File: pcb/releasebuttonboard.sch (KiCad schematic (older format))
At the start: 24 parts

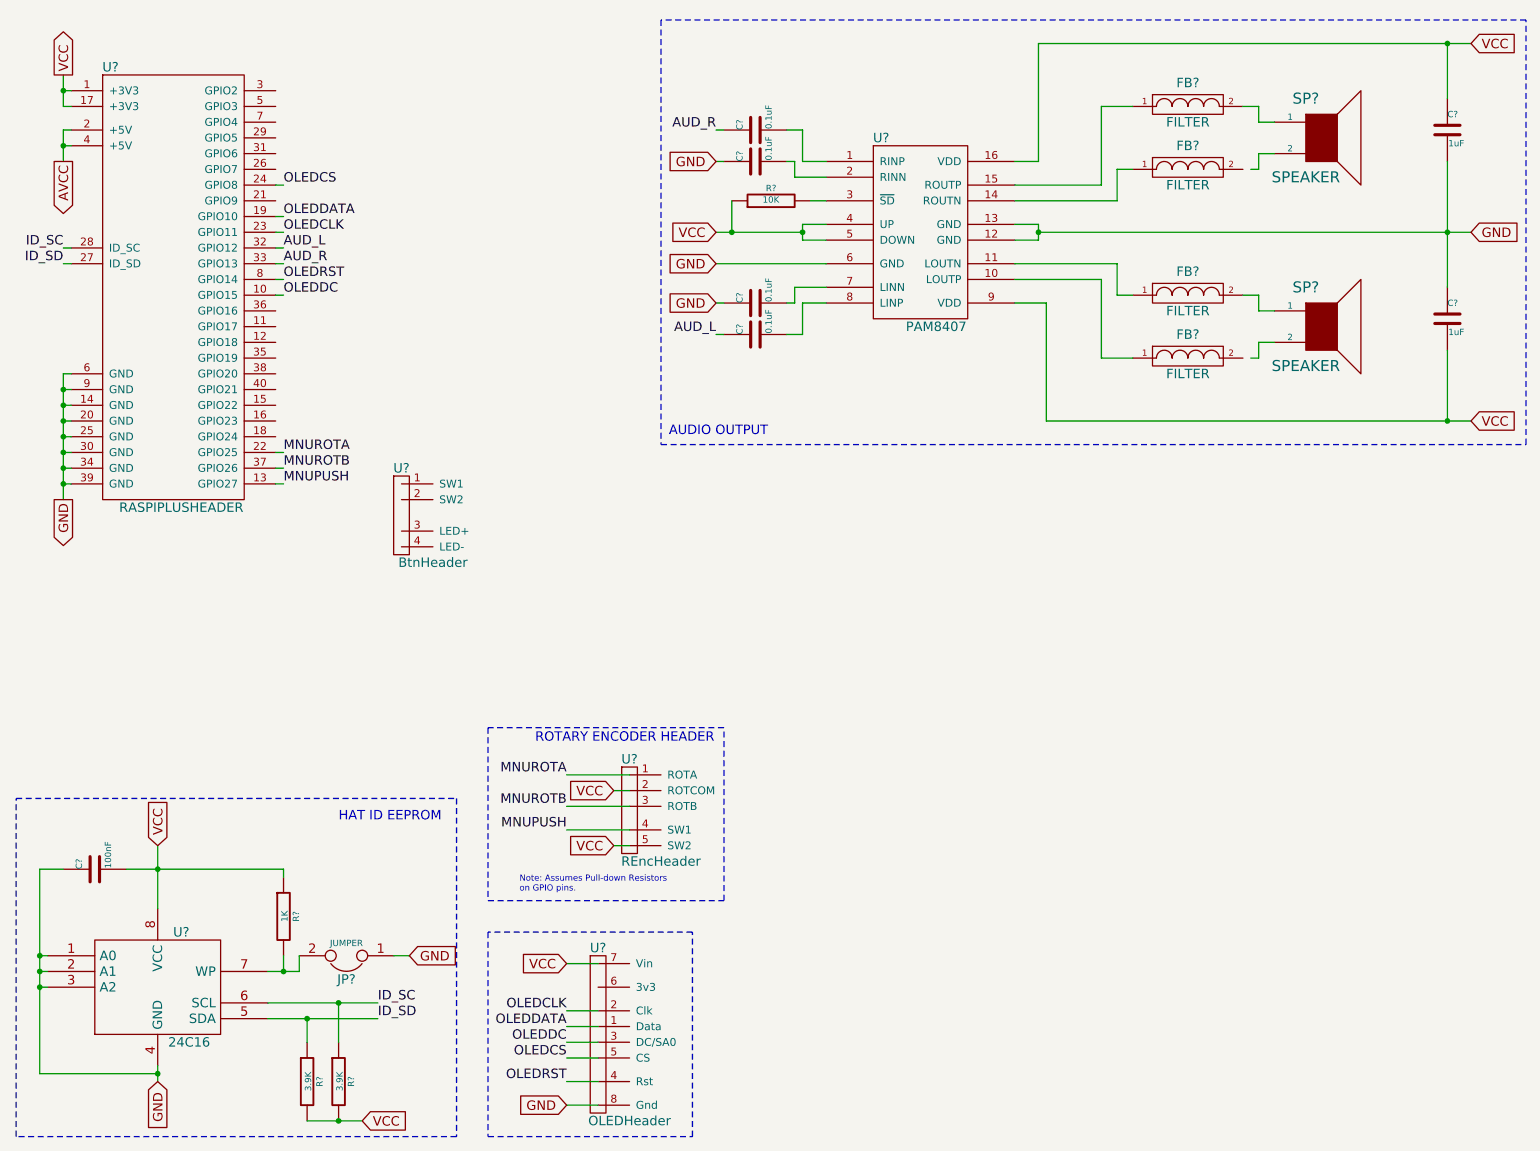
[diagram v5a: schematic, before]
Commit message: Header for big button.
(Plus misc schematic layout changes.)
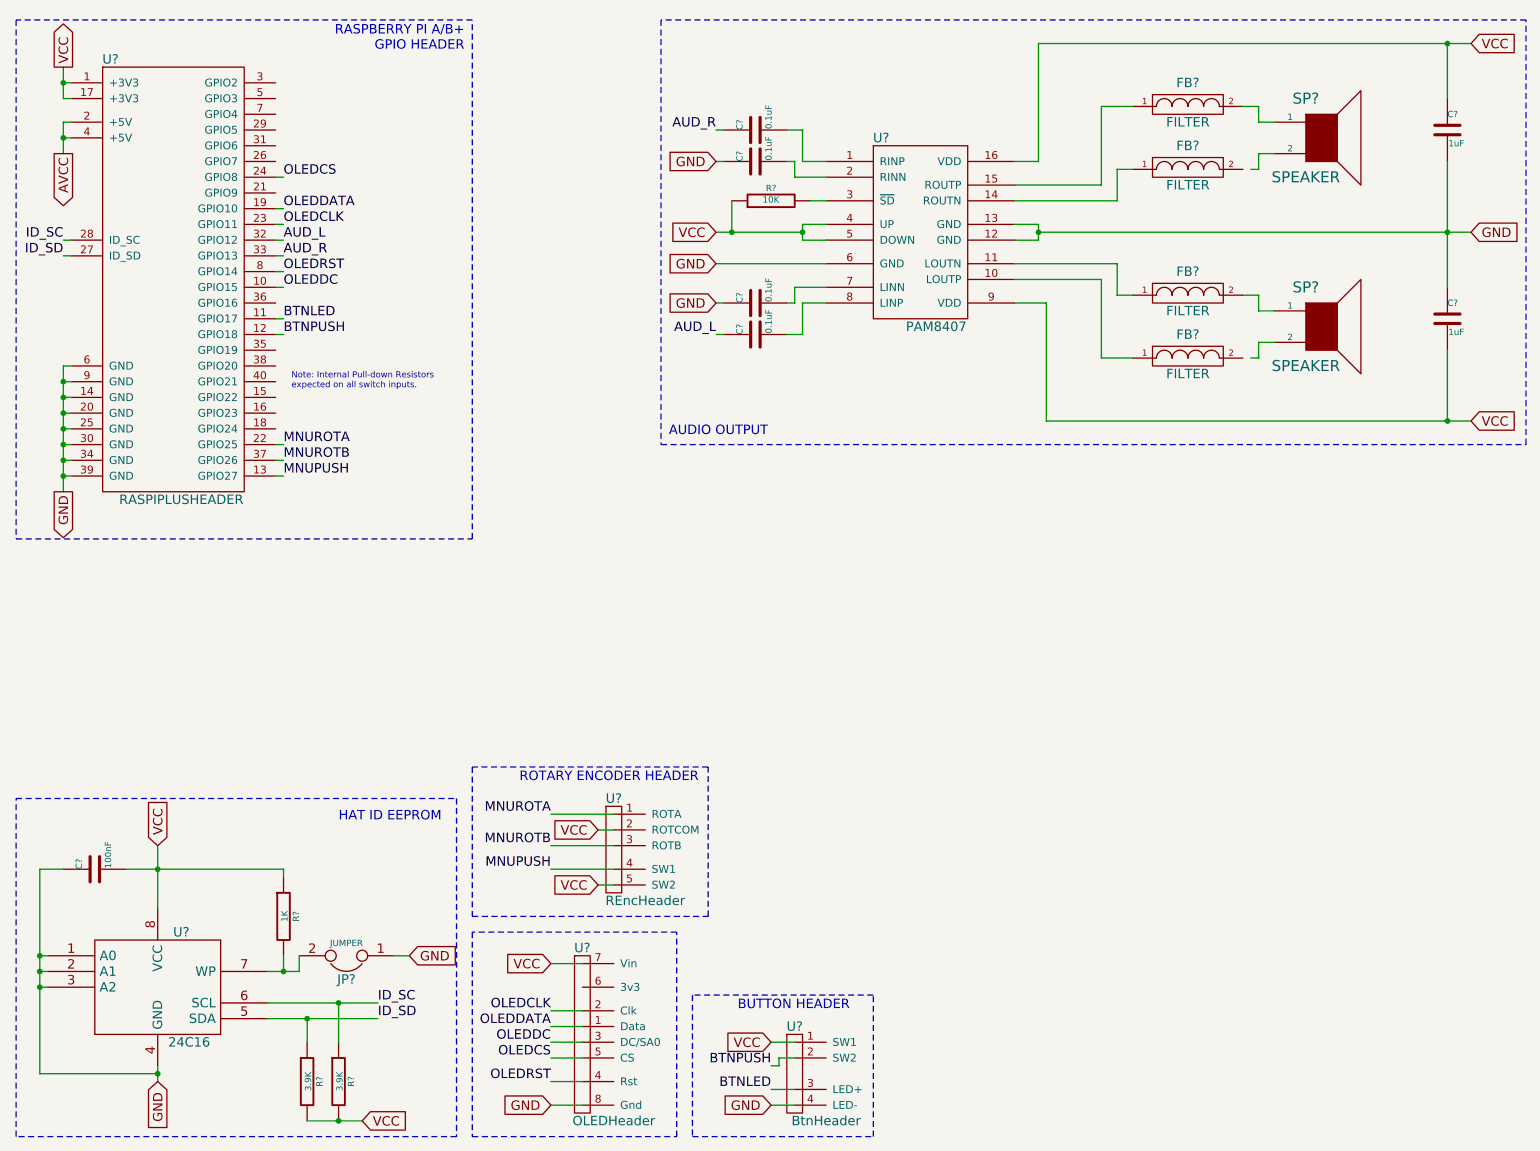
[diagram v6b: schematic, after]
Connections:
- net GND: now also U?.4 (LED-)
- net VCC: now also U?.1 (SW1)
- net BTNLED: now reaches U?.11 (GPIO17)
- net BTNLED: now also U?.3 (LED+)
- net BTNPUSH: now reaches U?.12 (GPIO18)
- net BTNPUSH: now also U?.2 (SW2)
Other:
- note added: "BUTTON HEADER"
- note added: "Note: Internal Pull-down Resistors\nexpected on all switch inputs."
- note added: "RASPBERRY PI A/B+\nGPIO HEADER"
- note removed: "Note: Assumes Pull-down Resistors\non GPIO pins."
- moved on the sheet: U?

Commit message: Component annotation.
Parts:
- gave numbers to parts that had none: 24
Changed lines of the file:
@@
 $EndDescr
 $Comp
-L RASPIPLUSHEADER U?
+L RASPIPLUSHEADER U2
 U 1 1 54A79B4A
 P 1700 2300
-F 0 "U?" H 1300 3650 60  0000 C CNN
+F 0 "U2" H 1300 3650 60  0000 C CNN
 F 1 "RASPIPLUSHEADER" H 1750 850 60  0000 C CNN
 F 2 "" H 1700 2050 60  0000 C CNN
@@
 $EndComp
 $Comp
-L OLEDHeader U?
+L OLEDHeader U3
 U 1 1 54A7A9C0
 P 4300 7100
-F 0 "U?" H 4300 7600 60  0000 C CNN
+F 0 "U3" H 4300 7600 60  0000 C CNN
 F 1 "OLEDHeader" H 4500 6500 60  0000 C CNN
 F 2 "" H 4300 7300 60  0000 C CNN
@@
 $EndComp
 $Comp
-L BtnHeader U?
+L BtnHeader U5
 U 1 1 54A7AA14
 P 5650 7400
-F 0 "U?" H 5650 7700 60  0000 C CNN
+F 0 "U5" H 5650 7700 60  0000 C CNN
 F 1 "BtnHeader" H 5850 7100 60  0000 C CNN
 F 2 "" H 5650 7450 60  0000 C CNN
@@
 $EndComp
 $Comp
-L REncHeader U?
+L REncHeader U4
 U 1 1 54A7ABB1
 P 4500 6000
-F 0 "U?" H 4500 6350 60  0000 C CNN
+F 0 "U4" H 4500 6350 60  0000 C CNN
 F 1 "REncHeader" H 4700 5700 60  0000 C CNN
 F 2 "" H 4500 6050 60  0000 C CNN
@@
 $EndComp
 $Comp
-L 24C16 U?
+L 24C16 U1
 U 1 1 54A83FFB
 P 1600 6850
-F 0 "U?" H 1750 7200 60  0000 C CNN
+F 0 "U1" H 1750 7200 60  0000 C CNN
 F 1 "24C16" H 1800 6500 60  0000 C CNN
 F 2 "" H 1600 6850 60  0000 C CNN
@@
 GND
 $Comp
-L JUMPER JP?
+L JUMPER JP1
 U 1 1 54A841ED
 P 2800 6650
-F 0 "JP?" H 2800 6800 60  0000 C CNN
+F 0 "JP1" H 2800 6800 60  0000 C CNN
 F 1 "JUMPER" H 2800 6570 40  0000 C CNN
 F 2 "" H 2800 6650 60  0000 C CNN
@@
 AUD_R
 $Comp
-L C C?
+L C C1
 U 1 1 54A8751D
 P 1200 6100
-F 0 "C?" H 1200 6200 40  0000 L CNN
+F 0 "C1" H 1200 6200 40  0000 L CNN
 F 1 "100nF" H 1206 6015 40  0000 L CNN
 F 2 "" H 1238 5950 30  0000 C CNN
@@
 $EndComp
 $Comp
-L R R?
+L R R1
 U 1 1 54A87661
 P 2400 6400
-F 0 "R?" V 2480 6400 40  0000 C CNN
+F 0 "R1" V 2480 6400 40  0000 C CNN
 F 1 "1K" V 2407 6401 40  0000 C CNN
 F 2 "" V 2330 6400 30  0000 C CNN
@@
 GND
 $Comp
-L R R?
+L R R2
 U 1 1 54A878B0
 P 2550 7450
-F 0 "R?" V 2630 7450 40  0000 C CNN
+F 0 "R2" V 2630 7450 40  0000 C CNN
 F 1 "3.9K" V 2557 7451 40  0000 C CNN
 F 2 "" V 2480 7450 30  0000 C CNN
@@
 $EndComp
 $Comp
-L R R?
+L R R3
 U 1 1 54A878C4
 P 2750 7450
-F 0 "R?" V 2830 7450 40  0000 C CNN
+F 0 "R3" V 2830 7450 40  0000 C CNN
 F 1 "3.9K" V 2757 7451 40  0000 C CNN
 F 2 "" V 2680 7450 30  0000 C CNN
@@
 VCC
 $Comp
-L FILTER FB?
+L FILTER FB1
 U 1 1 54A87BC1
 P 8150 1250
-F 0 "FB?" H 8150 1400 60  0000 C CNN
+F 0 "FB1" H 8150 1400 60  0000 C CNN
 F 1 "FILTER" H 8150 1150 60  0000 C CNN
 F 2 "" H 8150 1250 60  0000 C CNN
@@
 $EndComp
 $Comp
-L FILTER FB?
+L FILTER FB2
 U 1 1 54A87BD5
 P 8150 1650
-F 0 "FB?" H 8150 1800 60  0000 C CNN
+F 0 "FB2" H 8150 1800 60  0000 C CNN
 F 1 "FILTER" H 8150 1550 60  0000 C CNN
 F 2 "" H 8150 1650 60  0000 C CNN
@@
 $EndComp
 $Comp
-L PAM8407 U?
+L PAM8407 U6
 U 1 1 54A880F4
 P 6450 2050
-F 0 "U?" H 6200 2650 60  0000 C CNN
+F 0 "U6" H 6200 2650 60  0000 C CNN
 F 1 "PAM8407" H 6550 1450 60  0000 C CNN
 F 2 "" H 6400 2150 60  0000 C CNN
@@
 GND
 $Comp
-L SPEAKER SP?
+L SPEAKER SP1
 U 1 1 54A88374
 P 9000 1450
-F 0 "SP?" H 8900 1700 70  0000 C CNN
+F 0 "SP1" H 8900 1700 70  0000 C CNN
 F 1 "SPEAKER" H 8900 1200 70  0000 C CNN
 F 2 "" H 9000 1450 60  0000 C CNN
@@
 $EndComp
 $Comp
-L FILTER FB?
+L FILTER FB3
 U 1 1 54A884E7
 P 8150 2450
-F 0 "FB?" H 8150 2600 60  0000 C CNN
+F 0 "FB3" H 8150 2600 60  0000 C CNN
 F 1 "FILTER" H 8150 2350 60  0000 C CNN
 F 2 "" H 8150 2450 60  0000 C CNN
@@
 $EndComp
 $Comp
-L FILTER FB?
+L FILTER FB4
 U 1 1 54A884ED
 P 8150 2850
-F 0 "FB?" H 8150 3000 60  0000 C CNN
+F 0 "FB4" H 8150 3000 60  0000 C CNN
 F 1 "FILTER" H 8150 2750 60  0000 C CNN
 F 2 "" H 8150 2850 60  0000 C CNN
@@
 $EndComp
 $Comp
-L SPEAKER SP?
+L SPEAKER SP2
 U 1 1 54A884F3
 P 9000 2650
-F 0 "SP?" H 8900 2900 70  0000 C CNN
+F 0 "SP2" H 8900 2900 70  0000 C CNN
 F 1 "SPEAKER" H 8900 2400 70  0000 C CNN
 F 2 "" H 9000 2650 60  0000 C CNN
@@
 VCC
 $Comp
-L C C?
+L C C6
 U 1 1 54A8854B
 P 9800 1400
-F 0 "C?" H 9800 1500 40  0000 L CNN
+F 0 "C6" H 9800 1500 40  0000 L CNN
 F 1 "1uF" H 9806 1315 40  0000 L CNN
 F 2 "" H 9838 1250 30  0000 C CNN
@@
 $EndComp
 $Comp
-L C C?
+L C C7
 U 1 1 54A8856C
 P 9800 2600
-F 0 "C?" H 9800 2700 40  0000 L CNN
+F 0 "C7" H 9800 2700 40  0000 L CNN
 F 1 "1uF" H 9806 2515 40  0000 L CNN
 F 2 "" H 9838 2450 30  0000 C CNN
@@
 VCC
 $Comp
-L R R?
+L R R4
 U 1 1 54A88EE7
 P 5500 1850
-F 0 "R?" V 5580 1850 40  0000 C CNN
+F 0 "R4" V 5580 1850 40  0000 C CNN
 F 1 "10K" V 5507 1851 40  0000 C CNN
 F 2 "" V 5430 1850 30  0000 C CNN
@@
 GND
 $Comp
-L C C?
+L C C3
 U 1 1 54A89346
 P 5400 1600
-F 0 "C?" H 5400 1700 40  0000 L CNN
+F 0 "C3" H 5400 1700 40  0000 L CNN
 F 1 "0.1uF" H 5406 1515 40  0000 L CNN
 F 2 "" H 5438 1450 30  0000 C CNN
@@
 $EndComp
 $Comp
-L C C?
+L C C2
 U 1 1 54A89373
 P 5400 1400
-F 0 "C?" H 5400 1500 40  0000 L CNN
+F 0 "C2" H 5400 1500 40  0000 L CNN
 F 1 "0.1uF" H 5406 1315 40  0000 L CNN
 F 2 "" H 5438 1250 30  0000 C CNN
@@
 $EndComp
 $Comp
-L C C?
+L C C4
 U 1 1 54A894DA
 P 5400 2500
-F 0 "C?" H 5400 2600 40  0000 L CNN
+F 0 "C4" H 5400 2600 40  0000 L CNN
 F 1 "0.1uF" H 5406 2415 40  0000 L CNN
 F 2 "" H 5438 2350 30  0000 C CNN
@@
 $EndComp
 $Comp
-L C C?
+L C C5
 U 1 1 54A894E5
 P 5400 2700
-F 0 "C?" H 5400 2800 40  0000 L CNN
+F 0 "C5" H 5400 2800 40  0000 L CNN
 F 1 "0.1uF" H 5406 2615 40  0000 L CNN
 F 2 "" H 5438 2550 30  0000 C CNN

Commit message: Remove unused AVCC label.
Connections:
- net AVCC: no longer names the net of U2.2 (+5V)
- net AVCC: no longer U2.4 (+5V)
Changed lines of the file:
@@
 	1    0    0    -1
 $EndComp
-Text GLabel 1000 1550 3    60   Output ~ 0
-AVCC
 Text GLabel 9950 850  2    60   Input ~ 0
 VCC
@@
 	700  7800 700  5650
 Wire Wire Line
-	1050 1450 1000 1450
-Wire Wire Line
-	1000 1350 1000 1550
-Wire Wire Line
-	1050 1350 1000 1350
-Connection ~ 1000 1450
-Wire Wire Line
 	8500 1250 8600 1250
